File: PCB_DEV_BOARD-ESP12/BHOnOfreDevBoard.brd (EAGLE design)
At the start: 48.4 x 47.7 mm, 22 parts, among them K1 OMRON-G3MB-202P-SSR2, K2 OMRON-G3MB-202P-SSR2, Q1 S8050, Q2 S8050

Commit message: Organização de ficheiros e versões do OnOfre, devenvolvimento da dev board
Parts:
- added J8, J9: (no value), SparkFun-Connectors:1X01
- moved J7 94.9 mm to (21.9, 48.1)
- moved J6 54.7 mm to (24.4, 24.0)
- moved R4 46.9 mm to (31.9, 3.48), turned to 90 degrees
- moved R1 45.7 mm to (38.4, 3.04)
- moved Q1 45.6 mm to (36.6, 13.2), turned to 90 degrees
- moved Q2 45.3 mm to (38.3, 5.64), turned to 90 degrees
- moved C4 42.1 mm to (12.9, 42.2), turned to 0 degrees
- moved K2 41.1 mm to (37.5, 9.68), turned to 0 degrees
- moved K1 37.5 mm to (37.5, 15.4), turned to 0 degrees
- moved D3 31.6 mm to (46.9, 21.9), turned to 270 degrees
- moved J2 29.1 mm to (39.7, 53.4), turned to 180 degrees
- moved R10 27.9 mm to (42.4, 45.5), turned to 0 degrees
- moved J3 26.0 mm to (39.6, 50.7), turned to 180 degrees
- moved F1 25.2 mm to (26.8, 3.23), turned to 0 degrees
- moved J4 24.6 mm to (42.2, 21.4), turned to 180 degrees
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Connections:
- removed net GND1: J4.1, J4.2, J4.3, J4.4, J4.5, J4.6, J4.7, J4.8
- removed net N$10: R11.1, U2.GPIO15
- net GPIO15: now also R11.1, U2.GPIO15
- net R1: now also J8.1
- net R2: now also J9.1
- net VCC: now also J4.1, J4.2, J4.3, J4.4, J4.5, J4.6, J4.7, J4.8
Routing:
- net VCC: track 16.9 -> 124.8 mm
- net GND: track 88.0 -> 182.8 mm
- net CH_PD: track 0.00 -> 27.2 mm
- net GPIO0: track 0.00 -> 22.7 mm
- net N$2: track 0.00 -> 21.5 mm
- net N$1: track 0.00 -> 14.6 mm
- net NEUTRAL_IN_FUSED: track 28.8 -> 14.3 mm
- net GPIO15: track 0.00 -> 12.2 mm
- net N$9: track 0.00 -> 11.1 mm
- net NEUTRAL_IN: track 33.6 -> 23.2 mm
- net N$7: track 0.00 -> 10.4 mm
- net TX: track 0.00 -> 7.98 mm
- net RESET: track 0.00 -> 7.31 mm
- net GPIO13: track 0.00 -> 5.00 mm
- net RX: track 0.00 -> 4.89 mm
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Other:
- board size 48.4 x 47.7 mm -> 53 x 55 mm

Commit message: Header pins para ligar os relés
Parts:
- moved J9 55.0 mm to (35.3, 3.42)
- moved J8 40.2 mm to (31.9, 1.48)
- moved R4 0.73 mm to (31.9, 4.21)
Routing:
- net R2: track 0.00 -> 2.59 mm
- net R1: track 0.00 -> 1.89 mm
- net N$7: track 10.4 -> 9.70 mm
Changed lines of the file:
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@@
 </element>
 <element name="Q1" library="semicon-smd-ipc" library_urn="urn:adsk.eagle:library:353" package="SOT23" package3d_urn="urn:adsk.eagle:package:26310/1" value="S8050 " x="36.61555625" y="13.1970125" rot="R90"/>
-<element name="R4" library="resistor" library_urn="urn:adsk.eagle:library:348" package="R0603" package3d_urn="urn:adsk.eagle:package:26057/1" value="47k" x="31.928028125" y="3.48493125" rot="R90"/>
+<element name="R4" library="resistor" library_urn="urn:adsk.eagle:library:348" package="R0603" package3d_urn="urn:adsk.eagle:package:26057/1" value="47k" x="31.928028125" y="4.2123625" rot="R90"/>
 <element name="U$2" library="PowerSocket" package="HLK-PM03" value="HLK-PM03" x="15.37839375" y="12.744771875" rot="R90"/>
 <element name="D3" library="Seeed-Diode" library_urn="urn:adsk.eagle:library:467" package="DO-214AC" package3d_urn="urn:adsk.eagle:package:32508/1" value="1N4004" x="46.90461875" y="21.878690625" rot="R270">
@@
 <attribute name="PROD_ID" value="CONN-08438" x="21.90115" y="48.146403125" size="1.778" layer="27" display="off"/>
 </element>
-<element name="J8" library="SparkFun-Connectors" library_urn="urn:adsk.eagle:library:513" package="1X01" package3d_urn="urn:adsk.eagle:package:38028/1" value="" x="-4.47360625" y="-15.703228125"/>
-<element name="J9" library="SparkFun-Connectors" library_urn="urn:adsk.eagle:library:513" package="1X01" package3d_urn="urn:adsk.eagle:package:38028/1" value="" x="-4.47360625" y="-34.499228125"/>
+<element name="J8" library="SparkFun-Connectors" library_urn="urn:adsk.eagle:library:513" package="1X01" package3d_urn="urn:adsk.eagle:package:38028/1" value="" x="31.8927375" y="1.484028125"/>
+<element name="J9" library="SparkFun-Connectors" library_urn="urn:adsk.eagle:library:513" package="1X01" package3d_urn="urn:adsk.eagle:package:38028/1" value="" x="35.29954375" y="3.4181375"/>
 </elements>
 <signals>
@@
 <contactref element="R4" pad="1"/>
 <contactref element="J8" pad="1"/>
-<wire x1="-4.47360625" y1="-15.703228125" x2="31.928028125" y2="2.63493125" width="0" layer="19" extent="1-1"/>
+<wire x1="31.8927375" y1="1.484028125" x2="31.8927375" y2="3.327071875" width="0.8128" layer="1"/>
+<wire x1="31.8927375" y1="3.327071875" x2="31.928028125" y2="3.3623625" width="0.8128" layer="1"/>
 </signal>
 <signal name="NEUTRAL_IN">
@@
 <contactref element="R1" pad="1"/>
 <contactref element="J9" pad="1"/>
-<wire x1="-4.47360625" y1="-34.499228125" x2="37.509059375" y2="3.038409375" width="0" layer="19" extent="1-1"/>
+<wire x1="37.509059375" y1="3.038409375" x2="37.509059375" y2="3.4181375" width="0.8128" layer="1"/>
+<wire x1="37.509059375" y1="3.4181375" x2="35.29954375" y2="3.4181375" width="0.8128" layer="1"/>
 </signal>
 <signal name="N$7">
 <contactref element="Q1" pad="1"/>
 <contactref element="R4" pad="2"/>
-<wire x1="31.928028125" y1="4.33493125" x2="31.928028125" y2="6.663815625" width="0.6096" layer="1"/>
+<wire x1="31.928028125" y1="5.0623625" x2="31.928028125" y2="6.663815625" width="0.6096" layer="1"/>
 <wire x1="31.928028125" y1="6.663815625" x2="33.000815625" y2="7.736603125" width="0.6096" layer="1"/>
 <wire x1="33.000815625" y1="7.736603125" x2="33.205146875" y2="7.736603125" width="0.6096" layer="1"/>

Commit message: melhoramentos nas pistas da dev board
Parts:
- added SW1: B3U-1000P-2P-SMD, Seeed-Switch:SW2-2.6-3.0X2.5X1.2+0.4MM
- moved J2 17.8 mm to (21.9, 53.6), turned to 0 degrees
- moved J4 17.7 mm to (24.4, 21.3), turned to 0 degrees
- moved J3 17.7 mm to (21.9, 50.9), turned to 0 degrees
- moved J5 0.26 mm to (24.4, 18.5)
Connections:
- net GND: now also SW1.2
- net RESET: now also SW1.1
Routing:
- net GND: track 182.8 -> 260.3 mm
- net VCC: track 124.8 -> 175.9 mm
- net RESET: track 7.31 -> 12.2 mm
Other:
- board text added: "BH OnOfre"
- board text added: "Dev Board"

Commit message: ficheiros para fazer a PCB na CNC
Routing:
- net VCC: track 175.9 -> 158.1 mm
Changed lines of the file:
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@@
 <layer number="23" name="tOrigins" color="15" fill="1" visible="yes" active="yes"/>
 <layer number="24" name="bOrigins" color="15" fill="1" visible="yes" active="yes"/>
-<layer number="25" name="tNames" color="7" fill="1" visible="no" active="yes"/>
-<layer number="26" name="bNames" color="7" fill="1" visible="no" active="yes"/>
-<layer number="27" name="tValues" color="7" fill="1" visible="no" active="yes"/>
+<layer number="25" name="tNames" color="7" fill="1" visible="yes" active="yes"/>
+<layer number="26" name="bNames" color="7" fill="1" visible="yes" active="yes"/>
+<layer number="27" name="tValues" color="7" fill="1" visible="yes" active="yes"/>
 <layer number="28" name="bValues" color="7" fill="1" visible="yes" active="yes"/>
 <layer number="29" name="tStop" color="7" fill="3" visible="no" active="yes"/>
@@
 <text x="6.99344375" y="16.011896875" size="2.54" layer="1" font="vector" rot="R90">BH OnOfre</text>
 <text x="11.73625625" y="18.18410625" size="2.54" layer="1" font="vector" rot="R90">Dev Board</text>
+<wire x1="53.19408125" y1="12.145271875" x2="41.19408125" y2="0.145271875" width="0.3048" layer="46"/>
+<wire x1="41.19408125" y1="0.145271875" x2="12.19408125" y2="0.145271875" width="0.3048" layer="46"/>
+<wire x1="12.19408125" y1="0.145271875" x2="0.19408125" y2="12.145271875" width="0.3048" layer="46"/>
+<wire x1="0.19408125" y1="12.145271875" x2="0.19408125" y2="24.145271875" width="0.3048" layer="46"/>
+<wire x1="0.19408125" y1="30.145271875" x2="0.19408125" y2="42.145271875" width="0.3048" layer="46"/>
+<wire x1="0.19408125" y1="42.145271875" x2="12.19408125" y2="55.145271875" width="0.3048" layer="46"/>
+<wire x1="12.19408125" y1="55.145271875" x2="41.19408125" y2="55.145271875" width="0.3048" layer="46"/>
+<wire x1="41.19408125" y1="55.145271875" x2="53.19408125" y2="42.145271875" width="0.3048" layer="46"/>
+<wire x1="53.19408125" y1="42.145271875" x2="53.19408125" y2="30.145271875" width="0.3048" layer="46"/>
+<wire x1="53.19408125" y1="24.145271875" x2="53.19408125" y2="12.145271875" width="0.3048" layer="46"/>
+<wire x1="53.19408125" y1="24.145271875" x2="53.19408125" y2="30.145271875" width="0.3048" layer="46" curve="-151.927513"/>
+<wire x1="0.19408125" y1="30.145271875" x2="0.19408125" y2="24.145271875" width="0.3048" layer="46" curve="-151.927513"/>
 </plain>
 <attributes>
@@
 <wire x1="34.60115" y1="50.88254375" x2="36.8927625" y2="50.88254375" width="0.6096" layer="1"/>
 <wire x1="37.14115" y1="50.88254375" x2="39.68115" y2="50.88254375" width="0.6096" layer="1"/>
-<wire x1="42.215521875" y1="21.25885" x2="24.435521875" y2="21.25885" width="0.8128" layer="1"/>
 </signal>
 <signal name="N$1">

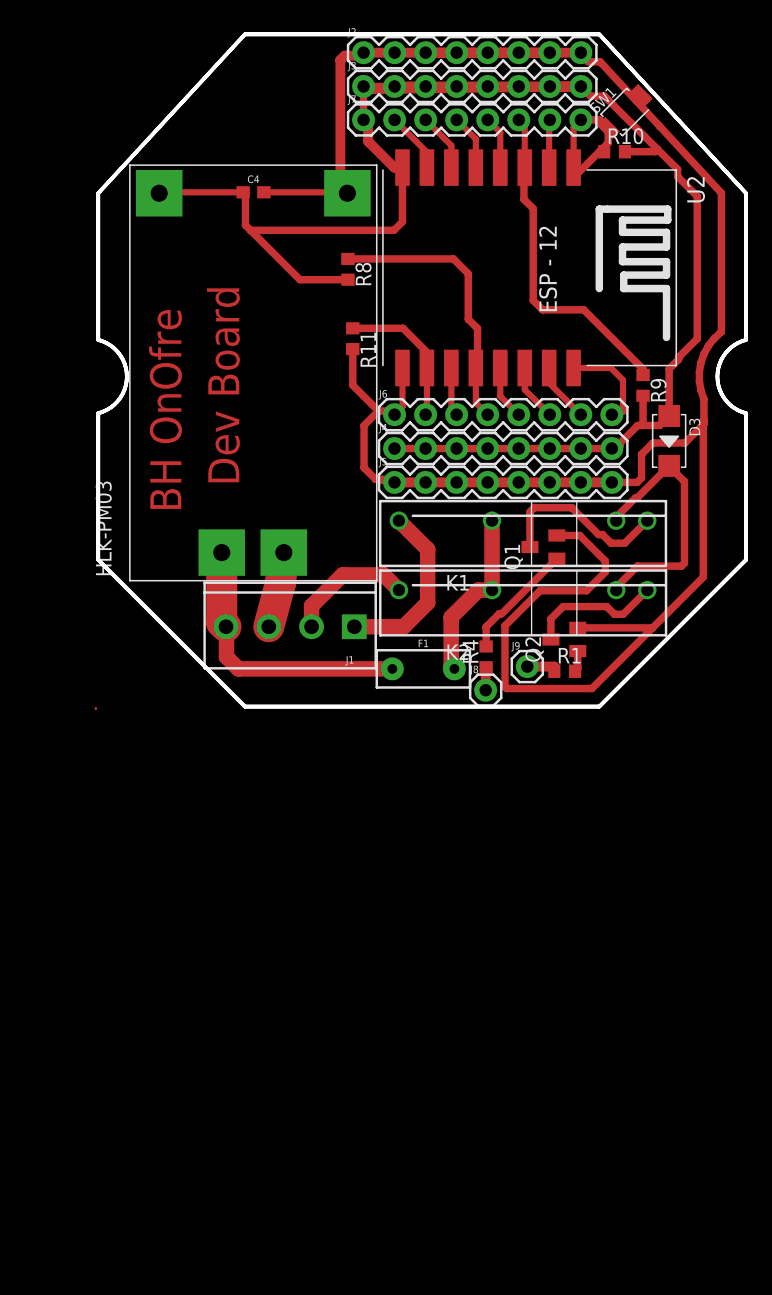
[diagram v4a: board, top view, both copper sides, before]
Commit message: problema de pull up dos relés resolvido, alteração  da fonte de 3.3v para 5v
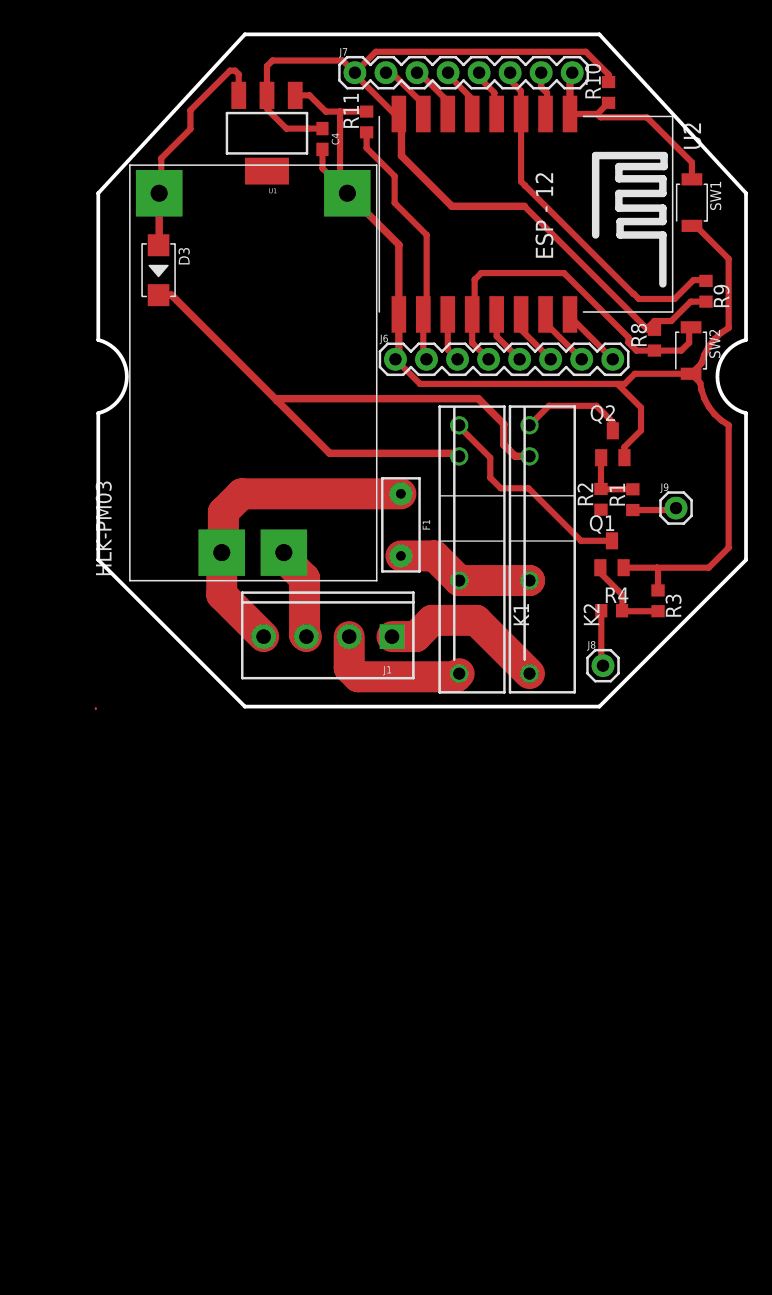
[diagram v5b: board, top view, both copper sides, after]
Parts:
- removed J2, J3, J4, J5: (no value), SparkFun-Connectors:1X08
- added R2, R3: 10k, resistor:R0603
- added SW2: B3U-1000P-2P-SMD, Seeed-Switch:SW2-2.6-3.0X2.5X1.2+0.4MM
- added U1: (no value), SparkFun-IC-Power:SOT223
- R1, R11, R4: value 47k -> 10k
- moved D3 44.1 mm to (5.13, 35.8)
- moved R8 25.7 mm to (45.7, 30.1), turned to 90 degrees
- moved J9 17.8 mm to (47.5, 16.4)
- moved R11 17.8 mm to (22.2, 48.0), turned to 90 degrees
- moved Q2 16.5 mm to (42.3, 21.6), turned to 0 degrees
- moved R1 15.1 mm to (43.9, 17.1), turned to 90 degrees
- moved F1 11.9 mm to (25.0, 15.0), turned to 270 degrees
- moved R4 10.9 mm to (42.2, 7.99), turned to 0 degrees
- moved J8 9.81 mm to (41.5, 3.49)
- moved R9 9.26 mm to (49.9, 34.1)
- moved SW1 9.23 mm to (48.8, 41.4), turned to 270 degrees
- moved K1 7.77 mm to (29.7, 15.5), turned to 90 degrees
- moved C4 7.13 mm to (18.5, 46.6), turned to 270 degrees
- moved K2 6.21 mm to (35.5, 15.5), turned to 90 degrees
- moved Q1 5.64 mm to (42.2, 12.6), turned to 0 degrees
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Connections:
- new net 3V3: C4.1, J7.1, R10.2, R8.2, R9.2, U1.2, U2.VCC
- net GND: now also R2.1, R3.1, SW2.2, U1.1; no longer J2.1, J2.2, J2.3, J2.4, J2.5, J2.6, J2.7, J2.8, J5.1, J5.2, J5.3, J5.4, J5.5, J5.6, J5.7, J5.8
- net GPIO0: now also SW2.1
- net N$13: now also R2.2
- net N$7: now also R3.2
- net NEUTRAL_ONE_OUT: now also J1.2; no longer J1.1
- net NEUTRAL_TWO_OUT: now also J1.1; no longer J1.2
- net VCC: now also U1.3; no longer C4.1, J3.1, J3.2, J3.3, J3.4, J3.5, J3.6, J3.7, J3.8, J4.1, J4.2, J4.3, J4.4, J4.5, J4.6, J4.7, J4.8, J7.1, R10.2, R8.2, R9.2, U2.VCC
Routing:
- net GND: track 260.3 -> 110.0 mm
- net VCC: track 158.1 -> 19.3 mm
- net 3V3: track 0.00 -> 80.7 mm
- net N$2: track 21.5 -> 53.7 mm
- net GPIO15: track 12.2 -> 21.0 mm
- net GPIO0: track 22.7 -> 29.4 mm
- net RESET: track 12.2 -> 18.0 mm
- net NEUTRAL_IN: track 23.2 -> 26.8 mm
- net N$13: track 1.74 -> 5.18 mm
- net NEUTRAL_TWO_OUT: track 10.4 -> 13.6 mm
- net NEUTRAL_IN_FUSED: track 14.3 -> 11.4 mm
- net TX: track 7.98 -> 5.12 mm
- net N$1: track 14.6 -> 17.4 mm
- net R1: track 1.89 -> 4.55 mm
- net NEUTRAL_ONE_OUT: track 14.5 -> 12.0 mm
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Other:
- board text removed: "BH OnOfre"
- board text removed: "Dev Board"

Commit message: no message
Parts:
- moved J8 0.44 mm to (41.4, 3.93)
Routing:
- net GND: track 110.0 -> 117.3 mm
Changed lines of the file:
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@@
 <attribute name="PROD_ID" value="CONN-08438" x="21.195303125" y="52.009259375" size="1.778" layer="27" display="off"/>
 </element>
-<element name="J8" library="SparkFun-Connectors" library_urn="urn:adsk.eagle:library:513" package="1X01" package3d_urn="urn:adsk.eagle:package:38028/1" value="" x="41.49235" y="3.49271875"/>
+<element name="J8" library="SparkFun-Connectors" library_urn="urn:adsk.eagle:library:513" package="1X01" package3d_urn="urn:adsk.eagle:package:38028/1" value="" x="41.443684375" y="3.93088125"/>
 <element name="J9" library="SparkFun-Connectors" library_urn="urn:adsk.eagle:library:513" package="1X01" package3d_urn="urn:adsk.eagle:package:38028/1" value="" x="47.4685375" y="16.388359375"/>
 <element name="SW1" library="Seeed-Switch" library_urn="urn:adsk.eagle:library:476" package="SW2-2.6-3.0X2.5X1.2+0.4MM" package3d_urn="urn:adsk.eagle:package:32999/1" value="B3U-1000P-2P-SMD" x="48.76858125" y="41.37954375" rot="R270">
@@
 <wire x1="44.60471875" y1="22.740496875" x2="44.60471875" y2="24.605290625" width="0.508" layer="1"/>
 <wire x1="44.60471875" y1="24.605290625" x2="42.667003125" y2="26.54300625" width="0.508" layer="1"/>
-<wire x1="45.90895" y1="11.508365625" x2="50.14511875" y2="11.508365625" width="0.508" layer="1"/>
+<wire x1="46.62123125" y1="11.508365625" x2="45.90895" y2="11.508365625" width="0.508" layer="1"/>
+<wire x1="46.62123125" y1="11.508365625" x2="50.14511875" y2="11.508365625" width="0.508" layer="1"/>
 <wire x1="45.90895" y1="11.508365625" x2="43.177525" y2="11.508365625" width="0.508" layer="1"/>
 <wire x1="50.14511875" y1="11.508365625" x2="51.771675" y2="13.134921875" width="0.508" layer="1"/>
@@
 <wire x1="18.53946875" y1="45.7348625" x2="18.53946875" y2="44.183696875" width="0.508" layer="1"/>
 <wire x1="18.53946875" y1="44.183696875" x2="21.2333625" y2="41.489803125" width="0.508" layer="1"/>
-<wire x1="43.24505625" y1="20.5089" x2="41.325925" y2="16.2535875" width="0" layer="19" extent="1-1"/>
+<wire x1="41.325925" y1="16.2535875" x2="41.483378125" y2="16.2535875" width="0.4064" layer="1"/>
+<wire x1="41.483378125" y1="16.2535875" x2="42.705728125" y2="15.0312375" width="0.4064" layer="1"/>
+<wire x1="42.705728125" y1="15.0312375" x2="43.098359375" y2="15.0312375" width="0.4064" layer="1"/>
+<wire x1="43.098359375" y1="15.0312375" x2="46.62123125" y2="11.508365625" width="0.4064" layer="1"/>
 </signal>
 <signal name="VCC">
@@
 <contactref element="J8" pad="1"/>
 <wire x1="41.35186875" y1="7.985690625" x2="41.35186875" y2="3.6332" width="0.508" layer="1"/>
-<wire x1="41.35186875" y1="3.6332" x2="41.49235" y2="3.49271875" width="0.508" layer="1"/>
+<wire x1="41.35186875" y1="3.6332" x2="41.443684375" y2="3.93088125" width="0.508" layer="1"/>
 </signal>
 <signal name="NEUTRAL_IN">
